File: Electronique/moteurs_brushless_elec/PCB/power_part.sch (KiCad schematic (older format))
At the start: 20 parts, among them J3 FAN, U4 B_Plug_5mm, U5 LM317_SOT223, U6 LM317_SOT223

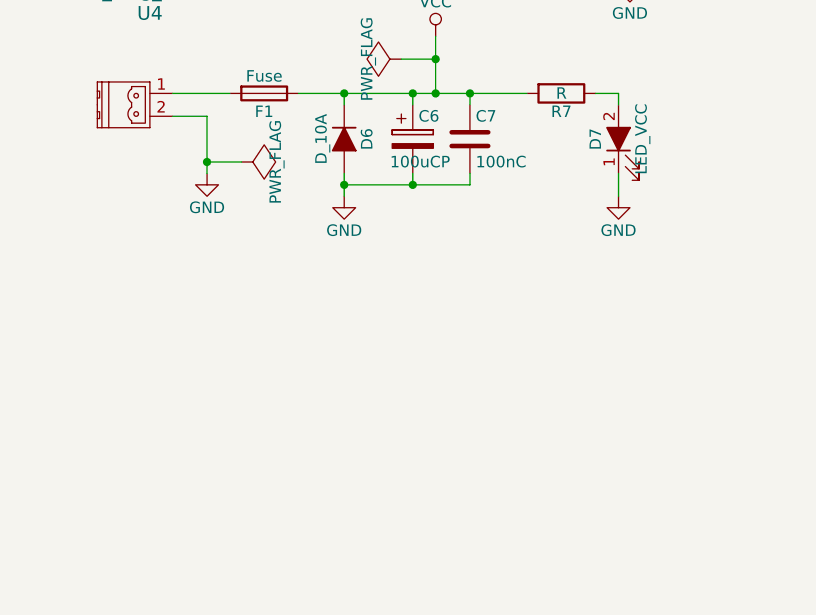
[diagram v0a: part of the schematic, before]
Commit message: rectification des empreintes
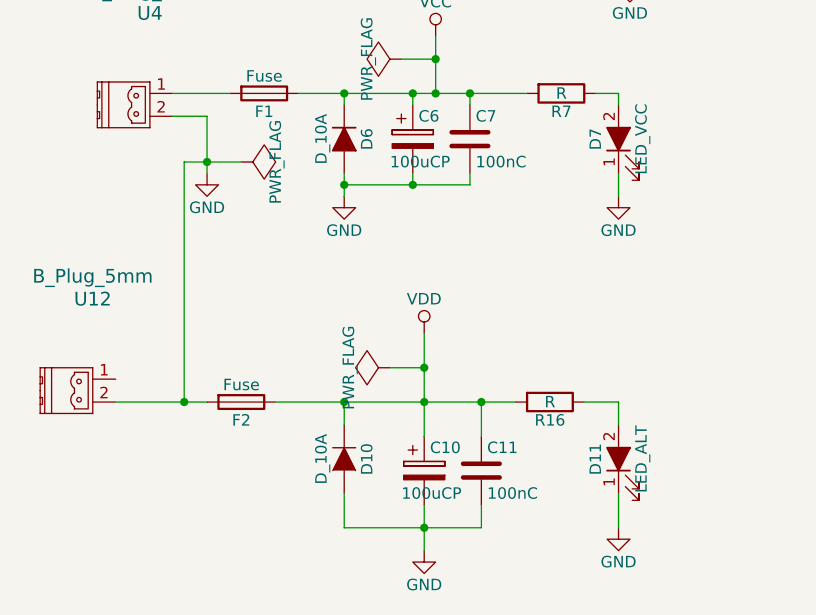
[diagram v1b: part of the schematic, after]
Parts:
- added C10: 100uCP, Capacitors_THT:CP_Radial_D8.0mm_P3.50mm, symbol CP
- added C11: 100nC, Capacitors_SMD:C_1206_HandSoldering, symbol C
- added D10: D_10A, Diodes_SMD:D_SMA_Handsoldering, symbol D
- added D11: LED_ALT, Diodes_SMD:D_SMA-SMB_Universal_Handsoldering, symbol LED_ALT
- added F2: Fuse, Fuse_Holders_and_Fuses:Fuseholder5x20_horiz_SemiClosed_Casing10x25mm, symbol Fuse
- added R16: R, Resistors_SMD:R_1206_HandSoldering, symbol R
- added U12: B_Plug_5mm, B plug:B plug 5mm, symbol B_Plug_5mm
- D6: footprint Diodes_SMD:D_SMC_Handsoldering -> Diodes_SMD:D_SMA_Handsoldering
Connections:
- net GND: now also C10.2, C11.2, D10.2 (A), D11.1 (K), F2.2, U12.2
- new net: D11.2 (A), R16.1
- new net VDD: C10.1, C11.1, D10.1 (K), F2.1, R16.2
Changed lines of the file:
@@
 $EndDescr
 $Comp
-L VCC #PWR042
+L VCC #PWR47
 U 1 1 5962E5D8
 P 4650 2300
-F 0 "#PWR042" H 4650 2150 50  0001 C CNN
+F 0 "#PWR47" H 4650 2150 50  0001 C CNN
 F 1 "VCC" H 4650 2450 50  0000 C CNN
 F 2 "" H 4650 2300 50  0001 C CNN
@@
 $EndComp
 $Comp
-L +3.3V #PWR043
+L +3.3V #PWR59
 U 1 1 5962E5EC
 P 10450 2450
-F 0 "#PWR043" H 10450 2300 50  0001 C CNN
+F 0 "#PWR59" H 10450 2300 50  0001 C CNN
 F 1 "+3.3V" H 10450 2590 50  0000 C CNN
 F 2 "" H 10450 2450 50  0001 C CNN
@@
 $EndComp
 $Comp
-L GND #PWR044
+L GND #PWR43
 U 1 1 5962E732
 P 3650 2900
-F 0 "#PWR044" H 3650 2650 50  0001 C CNN
+F 0 "#PWR43" H 3650 2650 50  0001 C CNN
 F 1 "GND" H 3650 2750 50  0000 C CNN
 F 2 "" H 3650 2900 50  0001 C CNN
@@
 F 0 "D6" H 4250 2850 50  0000 C CNN
 F 1 "D_10A" H 4250 2650 50  0000 C CNN
-F 2 "Diodes_SMD:D_SMC_Handsoldering" H 4250 2750 50  0001 C CNN
+F 2 "Diodes_SMD:D_SMA_Handsoldering" H 4250 2750 50  0001 C CNN
 F 3 "" H 4250 2750 50  0001 C CNN
 	1    4250 2750
@@
 $EndComp
 $Comp
-L GND #PWR045
+L GND #PWR44
 U 1 1 5962E829
 P 4250 3000
-F 0 "#PWR045" H 4250 2750 50  0001 C CNN
+F 0 "#PWR44" H 4250 2750 50  0001 C CNN
 F 1 "GND" H 4250 2850 50  0000 C CNN
 F 2 "" H 4250 3000 50  0001 C CNN
@@
 	3650 2650 3650 2900
 $Comp
-L PWR_FLAG #FLG046
+L PWR_FLAG #FLG3
 U 1 1 5962EB73
 P 4500 2400
-F 0 "#FLG046" H 4500 2475 50  0001 C CNN
+F 0 "#FLG3" H 4500 2475 50  0001 C CNN
 F 1 "PWR_FLAG" H 4500 2550 50  0000 C CNN
 F 2 "" H 4500 2400 50  0001 C CNN
@@
 $EndComp
 $Comp
-L PWR_FLAG #FLG047
+L PWR_FLAG #FLG1
 U 1 1 5962EBA1
 P 3800 2850
-F 0 "#FLG047" H 3800 2925 50  0001 C CNN
+F 0 "#FLG1" H 3800 2925 50  0001 C CNN
 F 1 "PWR_FLAG" H 3800 3000 50  0000 C CNN
 F 2 "" H 3800 2850 50  0001 C CNN
@@
 $EndComp
 Wire Wire Line
-	3800 2850 3650 2850
+	3550 2850 3800 2850
 Connection ~ 3650 2850
 $Comp
-L +5V #PWR048
+L +5V #PWR54
 U 1 1 5962ECD4
 P 7900 2450
-F 0 "#PWR048" H 7900 2300 50  0001 C CNN
+F 0 "#PWR54" H 7900 2300 50  0001 C CNN
 F 1 "+5V" H 7900 2590 50  0000 C CNN
 F 2 "" H 7900 2450 50  0001 C CNN
@@
 $EndComp
 $Comp
-L VCC #PWR049
+L VCC #PWR52
 U 1 1 5962F11A
 P 6450 2450
-F 0 "#PWR049" H 6450 2300 50  0001 C CNN
+F 0 "#PWR52" H 6450 2300 50  0001 C CNN
 F 1 "VCC" H 6450 2600 50  0000 C CNN
 F 2 "" H 6450 2450 50  0001 C CNN
@@
 $EndComp
 $Comp
-L VCC #PWR050
+L VCC #PWR57
 U 1 1 5962F138
 P 9050 2450
-F 0 "#PWR050" H 9050 2300 50  0001 C CNN
+F 0 "#PWR57" H 9050 2300 50  0001 C CNN
 F 1 "VCC" H 9050 2600 50  0000 C CNN
 F 2 "" H 9050 2450 50  0001 C CNN
@@
 $EndComp
 $Comp
-L GND #PWR051
+L GND #PWR53
 U 1 1 5962F3CB
 P 7000 3600
-F 0 "#PWR051" H 7000 3350 50  0001 C CNN
+F 0 "#PWR53" H 7000 3350 50  0001 C CNN
 F 1 "GND" H 7000 3450 50  0000 C CNN
 F 2 "" H 7000 3600 50  0001 C CNN
@@
 $EndComp
 $Comp
-L GND #PWR052
+L GND #PWR58
 U 1 1 5962F3F1
 P 9650 3600
-F 0 "#PWR052" H 9650 3350 50  0001 C CNN
+F 0 "#PWR58" H 9650 3350 50  0001 C CNN
 F 1 "GND" H 9650 3450 50  0000 C CNN
 F 2 "" H 9650 3600 50  0001 C CNN
@@
 $EndComp
 $Comp
-L GND #PWR053
+L GND #PWR48
 U 1 1 5963063C
 P 5450 3000
-F 0 "#PWR053" H 5450 2750 50  0001 C CNN
+F 0 "#PWR48" H 5450 2750 50  0001 C CNN
 F 1 "GND" H 5450 2850 50  0000 C CNN
 F 2 "" H 5450 3000 50  0001 C CNN
@@
 $EndComp
 $Comp
-L GND #PWR054
+L GND #PWR56
 U 1 1 5963066E
 P 8400 3100
-F 0 "#PWR054" H 8400 2850 50  0001 C CNN
+F 0 "#PWR56" H 8400 2850 50  0001 C CNN
 F 1 "GND" H 8400 2950 50  0000 C CNN
 F 2 "" H 8400 3100 50  0001 C CNN
@@
 $EndComp
 $Comp
-L GND #PWR055
+L GND #PWR61
 U 1 1 596306A0
 P 10850 3100
-F 0 "#PWR055" H 10850 2850 50  0001 C CNN
+F 0 "#PWR61" H 10850 2850 50  0001 C CNN
 F 1 "GND" H 10850 2950 50  0000 C CNN
 F 2 "" H 10850 3100 50  0001 C CNN
@@
 $EndComp
 $Comp
-L GND #PWR056
+L GND #PWR55
 U 1 1 596262B8
 P 7900 3300
-F 0 "#PWR056" H 7900 3050 50  0001 C CNN
+F 0 "#PWR55" H 7900 3050 50  0001 C CNN
 F 1 "GND" H 7900 3150 50  0000 C CNN
 F 2 "" H 7900 3300 50  0001 C CNN
@@
 $EndComp
 $Comp
-L GND #PWR057
+L GND #PWR60
 U 1 1 5962633A
 P 10450 3350
-F 0 "#PWR057" H 10450 3100 50  0001 C CNN
+F 0 "#PWR60" H 10450 3100 50  0001 C CNN
 F 1 "GND" H 10450 3200 50  0000 C CNN
 F 2 "" H 10450 3350 50  0001 C CNN
@@
 $EndComp
 $Comp
-L GND #PWR058
+L GND #PWR51
 U 1 1 596AA4A9
 P 5500 2050
-F 0 "#PWR058" H 5500 1800 50  0001 C CNN
+F 0 "#PWR51" H 5500 1800 50  0001 C CNN
 F 1 "GND" H 5500 1900 50  0000 C CNN
 F 2 "" H 5500 2050 50  0001 C CNN
@@
 $EndComp
 $Comp
-L VCC #PWR059
+L VCC #PWR50
 U 1 1 596AA4E5
 P 5500 1850
-F 0 "#PWR059" H 5500 1700 50  0001 C CNN
+F 0 "#PWR50" H 5500 1700 50  0001 C CNN
 F 1 "VCC" H 5500 2000 50  0000 C CNN
 F 2 "" H 5500 1850 50  0001 C CNN
@@
 Wire Wire Line
 	5500 2000 5600 2000
+$Comp
+L B_Plug_5mm U12
+U 1 1 5A34421A
+P 3150 3850
+F 0 "U12" H 3150 4250 60  0000 C CNN
+F 1 "B_Plug_5mm" H 3150 4350 60  0000 C CNN
+F 2 "B plug:B plug 5mm" H 3150 3850 60  0001 C CNN
+F 3 "" H 3150 3850 60  0000 C CNN
+	1    3150 3850
+	1    0    0    -1
+$EndComp
+Wire Wire Line
+	3250 3900 3650 3900
+Wire Wire Line
+	3550 3900 3550 2850
+$Comp
+L Fuse F2
+U 1 1 5A3442DC
+P 3800 3900
+F 0 "F2" V 3880 3900 50  0000 C CNN
+F 1 "Fuse" V 3725 3900 50  0000 C CNN
+F 2 "Fuse_Holders_and_Fuses:Fuseholder5x20_horiz_SemiClosed_Casing10x25mm" V 3730 3900 50  0001 C CNN
+F 3 "" H 3800 3900 50  0001 C CNN
+	1    3800 3900
+	0    1    1    0
+$EndComp
+$Comp
+L D D10
+U 1 1 5A344361
+P 4250 4150
+F 0 "D10" H 4250 4250 50  0000 C CNN
+F 1 "D_10A" H 4250 4050 50  0000 C CNN
+F 2 "Diodes_SMD:D_SMA_Handsoldering" H 4250 4150 50  0001 C CNN
+F 3 "" H 4250 4150 50  0000 C CNN
+	1    4250 4150
+	0    1    1    0
+$EndComp
+$Comp
+L C C11
+U 1 1 5A344493
+P 4850 4200
+F 0 "C11" H 4875 4300 50  0000 L CNN
+F 1 "100nC" H 4875 4100 50  0000 L CNN
+F 2 "Capacitors_SMD:C_1206_HandSoldering" H 4888 4050 50  0001 C CNN
+F 3 "" H 4850 4200 50  0000 C CNN
+	1    4850 4200
+	1    0    0    -1
+$EndComp
+$Comp
+L CP C10
+U 1 1 5A344500
+P 4600 4200
+F 0 "C10" H 4625 4300 50  0000 L CNN
+F 1 "100uCP" H 4500 4100 50  0000 L CNN
+F 2 "Capacitors_THT:CP_Radial_D8.0mm_P3.50mm" H 4638 4050 50  0001 C CNN
+F 3 "" H 4600 4200 50  0000 C CNN
+	1    4600 4200
+	1    0    0    -1
+$EndComp
+$Comp
+L R R16
+U 1 1 5A344571
+P 5150 3900
+F 0 "R16" V 5230 3900 50  0000 C CNN
+F 1 "R" V 5150 3900 50  0000 C CNN
+F 2 "Resistors_SMD:R_1206_HandSoldering" V 5080 3900 50  0001 C CNN
+F 3 "" H 5150 3900 50  0000 C CNN
+	1    5150 3900
+	0    1    1    0
+$EndComp
+$Comp
+L LED_ALT D11
+U 1 1 5A34463F
+P 5450 4150
+F 0 "D11" H 5450 4250 50  0000 C CNN
+F 1 "LED_ALT" H 5450 4050 50  0000 C CNN
+F 2 "Diodes_SMD:D_SMA-SMB_Universal_Handsoldering" H 5450 4150 50  0001 C CNN
+F 3 "" H 5450 4150 50  0001 C CNN
+	1    5450 4150
+	0    -1   -1   0
+$EndComp
+$Comp
+L GND #PWR49
+U 1 1 5A3446EC
+P 5450 4450
+F 0 "#PWR49" H 5450 4200 50  0001 C CNN
+F 1 "GND" H 5450 4300 50  0000 C CNN
+F 2 "" H 5450 4450 50  0000 C CNN
+F 3 "" H 5450 4450 50  0000 C CNN
+	1    5450 4450
+	1    0    0    -1
+$EndComp
+$Comp
+L GND #PWR46
+U 1 1 5A344736
+P 4600 4550
+F 0 "#PWR46" H 4600 4300 50  0001 C CNN
+F 1 "GND" H 4600 4400 50  0000 C CNN
+F 2 "" H 4600 4550 50  0000 C CNN
+F 3 "" H 4600 4550 50  0000 C CNN
+	1    4600 4550
+	1    0    0    -1
+$EndComp
+Connection ~ 3550 3900
+Wire Wire Line
+	3950 3900 5000 3900
+Wire Wire Line
+	5300 3900 5450 3900
+Wire Wire Line
+	5450 3900 5450 4000
+Wire Wire Line
+	5450 4300 5450 4450
+Wire Wire Line
+	4600 4550 4600 4350
+Wire Wire Line
+	4250 4300 4250 4450
+Wire Wire Line
+	4250 4450 4850 4450
+Connection ~ 4600 4450
+Wire Wire Line
+	4850 4450 4850 4350
+Wire Wire Line
+	4250 4000 4250 3900
+Connection ~ 4250 3900
+Wire Wire Line
+	4600 3600 4600 4050
+Connection ~ 4600 3900
+Wire Wire Line
+	4850 4050 4850 3900
+Connection ~ 4850 3900
+$Comp
+L VDD #PWR45
+U 1 1 5A345F99
+P 4600 3600
+F 0 "#PWR45" H 4600 3450 50  0001 C CNN
+F 1 "VDD" H 4600 3750 50  0000 C CNN
+F 2 "" H 4600 3600 50  0000 C CNN
+F 3 "" H 4600 3600 50  0000 C CNN
+	1    4600 3600
+	1    0    0    -1
+$EndComp
+$Comp
+L PWR_FLAG #FLG2
+U 1 1 5A345FE3
+P 4450 3750
+F 0 "#FLG2" H 4450 3845 50  0001 C CNN
+F 1 "PWR_FLAG" H 4450 3930 50  0000 C CNN
+F 2 "" H 4450 3750 50  0000 C CNN
+F 3 "" H 4450 3750 50  0000 C CNN
+	1    4450 3750
+	0    -1   -1   0
+$EndComp
+Wire Wire Line
+	4450 3750 4600 3750
+Connection ~ 4600 3750
 $EndSCHEMATC
